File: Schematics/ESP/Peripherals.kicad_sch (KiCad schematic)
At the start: 44 parts, among them J12 Battery Input, J3 Battery charger, J4 Motor A, J5 Motor B, J6 Fan, Q17 PJP18N20, SW1 SW_SPDT, U4 DRV8871DDA, U5 LM2596S-5, U6 DRV8871DDA

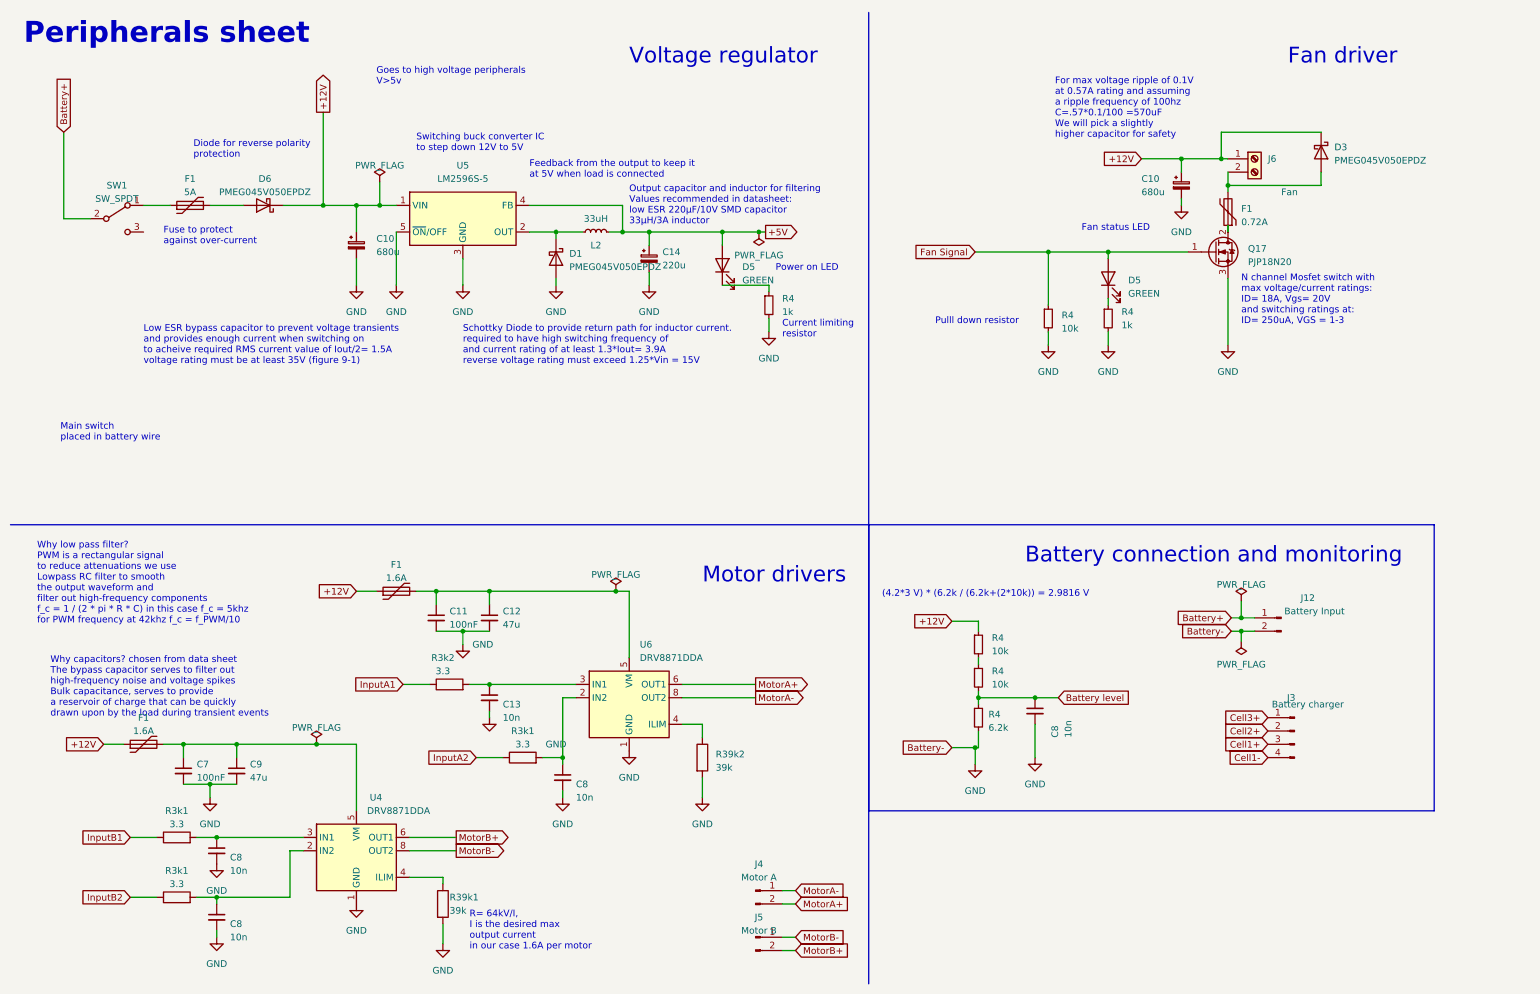
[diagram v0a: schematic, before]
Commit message: added esp32 connected
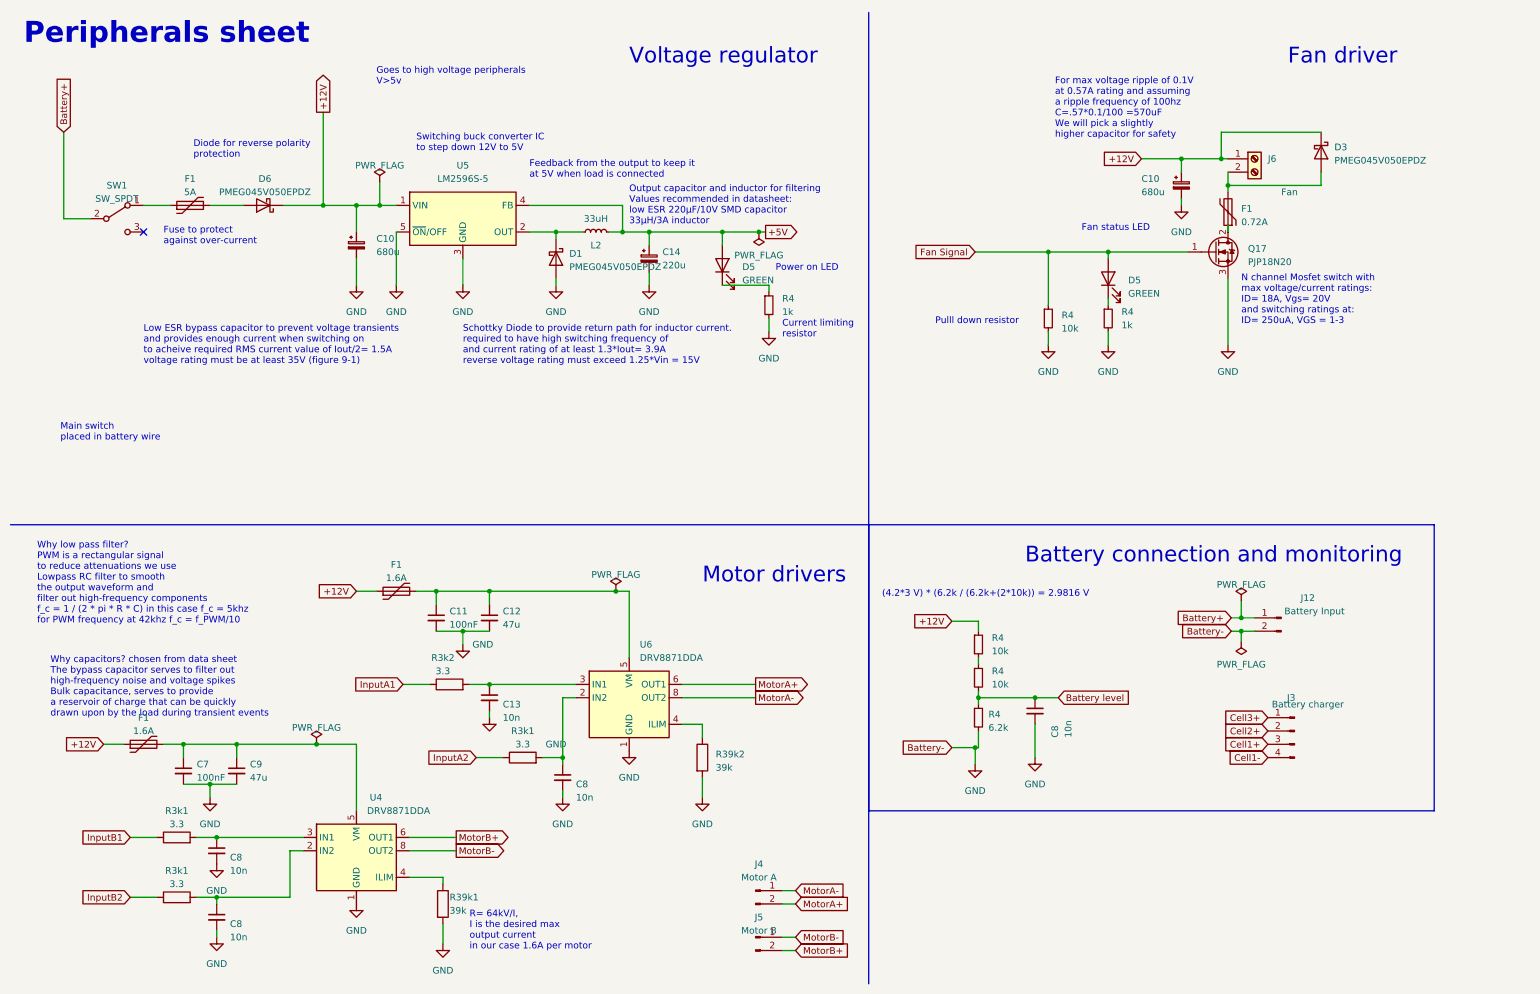
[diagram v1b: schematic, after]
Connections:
- no-connect marks 0 -> 1
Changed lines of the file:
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@@
   (junction (at 99.06 130.81) (diameter 0) (color 0 0 0 0)
   )
+  (no_connect (at 38.1 54.61))
   (wire (pts (xy 64.77 49.53) (xy 72.39 49.53))
     (stroke (width 0) (type default))
@@
     (stroke (width 0) (type default))
   )
-  (wire (pts (xy 196.85 153.035) (xy 192.405 153.035))
-    (stroke (width 0) (type default))
-  )
   (wire (pts (xy 245.745 128.27) (xy 247.65 128.27))
     (stroke (width 0) (type default))
@@
     (stroke (width 0) (type default))
   )
+  (wire (pts (xy 192.405 153.035) (xy 196.85 153.035))
+    (stroke (width 0) (type default))
+  )
   (wire (pts (xy 127 54.61) (xy 129.54 54.61))
     (stroke (width 0) (type default))
@@
     (stroke (width 0) (type default))
   )
-  (wire (pts (xy 196.85 156.21) (xy 196.85 153.035))
-    (stroke (width 0) (type default))
-  )
+  (wire (pts (xy 196.85 153.035) (xy 196.85 156.21))
+    (stroke (width 0) (type default))
+  )

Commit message: fixed bom
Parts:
- F1: Price 0,39 -> 0,32; digikey link https://www.digikey.fi/en/products/detail/bel-fuse-inc/0ZCG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 -> https://www.digikey.com/en/products/detail/bel-fuse-inc/068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
- J12, J3: digikey link (none) -> https://www.digikey.com/en/products/detail/sullins-connecto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
- SW1: digikey link (none) -> https://www.digikey.fi/fi/products/detail/e-switch/500SSP1S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
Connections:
- net Cell1- is gone; now on net GND: J3.4 (Pin_4)
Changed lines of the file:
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@@
+    )
+  )
+  (global_label "Battery-" (shape input) (at 252.73 154.94 180) (fields_autoplaced)
+    (effects (font (size 1.27 1.27)) (justify right))
+    (property "Intersheetrefs" "${INTERSHEET_REFS}" (at 241.539 154.94 0)
+      (effects (font (size 1.27 1.27)) (justify right) hide)
     )
   )
@@
     (property "Intersheetrefs" "${INTERSHEET_REFS}" (at 165.2755 143.4306 0)
       (effects (font (size 1.27 1.27)) (justify left) hide)
-    )
-  )
-  (global_label "Cell1-" (shape input) (at 252.73 154.94 180) (fields_autoplaced)
-    (effects (font (size 1.27 1.27)) (justify right))
-    (property "Intersheetrefs" "${INTERSHEET_REFS}" (at 243.3533 154.94 0)
-      (effects (font (size 1.27 1.27)) (justify right) hide)
     )
   )
@@
       (effects (font (size 1.27 1.27)) hide)
     )
+    (property "digikey link" "https://www.digikey.com/en/products/detail/sullins-connector-solutions/PPTC041LFBN-RC/810144" (at 257.81 149.86 0)
+      (effects (font (size 1.27 1.27)) hide)
+    )
     (pin "1")
     (pin "2")
@@
       (effects (font (size 1.27 1.27)) hide)
     )
-    (property "digikey link" "https://www.digikey.fi/en/products/detail/bel-fuse-inc/0ZCG0260BF2B/4156115" (at 46.99 49.53 90)
-      (effects (font (size 1.27 1.27)) hide)
-    )
-    (property "Price" "0,39" (at 46.99 49.53 0)
+    (property "digikey link" "https://www.digikey.com/en/products/detail/bel-fuse-inc/0685T5000-01/5466711?s=N4IgTCBcDaIAwDYAcBWAKiuWC0cCMIAugL5A" (at 46.99 49.53 90)
+      (effects (font (size 1.27 1.27)) hide)
+    )
+    (property "Price" "0,32" (at 46.99 49.53 0)
       (effects (font (size 1.27 1.27)) hide)
     )
@@
       (effects (font (size 1.27 1.27)) hide)
     )
+    (property "digikey link" "https://www.digikey.com/en/products/detail/sullins-connector-solutions/PPTC021LFBN-RC/810142" (at 255.27 128.27 0)
+      (effects (font (size 1.27 1.27)) hide)
+    )
     (pin "1")
     (pin "2")
@@
       (effects (font (size 1.27 1.27)) hide)
     )
+    (property "digikey link" "https://www.digikey.fi/fi/products/detail/e-switch/500SSP1S1M6QEA/378947?s=N4IgTCBcDaIKwAYEGVkAUCMyMFkBsAigKICCIAugL5A" (at 33.02 52.07 0)
+      (effects (font (size 1.27 1.27)) hide)
+    )

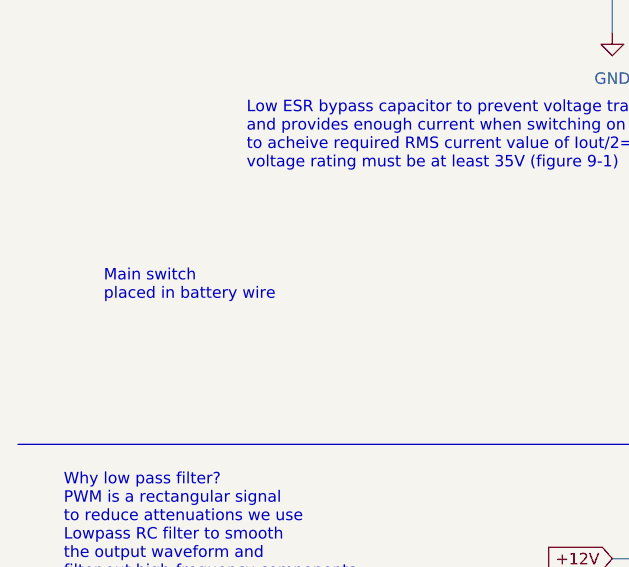
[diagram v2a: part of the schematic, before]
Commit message: charging IC PCB and cleanup
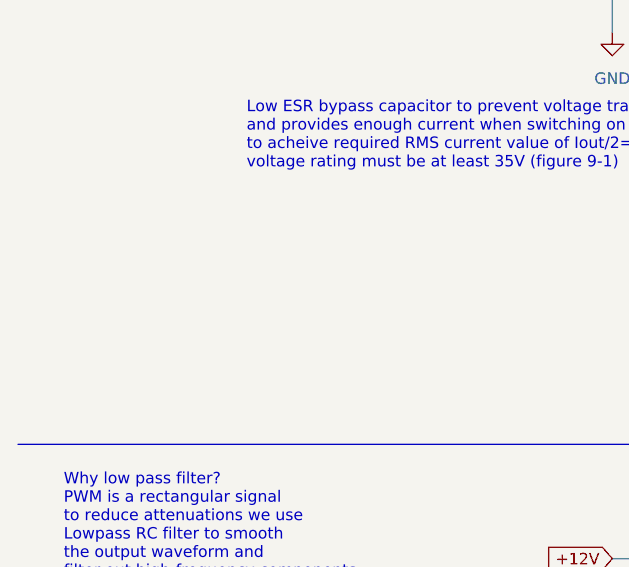
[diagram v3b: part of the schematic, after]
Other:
- note removed: "Main switch placed in battery wire"
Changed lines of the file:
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@@
     (effects (font (size 3 3)) (justify left bottom))
-  )
-  (text "Main switch\nplaced in battery wire" (at 22.225 94.615 0)
-    (effects (font (size 1.27 1.27)) (justify left bottom))
   )
   (text "Feedback from the output to keep it \nat 5V when load is connected"

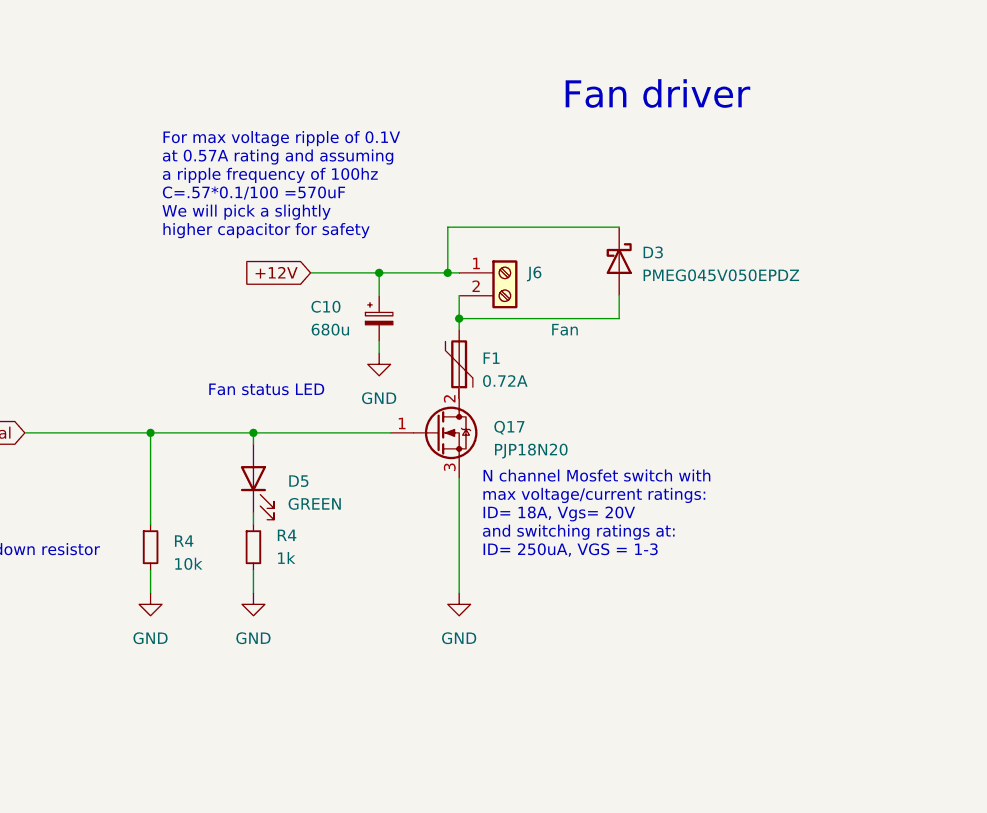
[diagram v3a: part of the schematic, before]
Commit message: removed fan related stuff
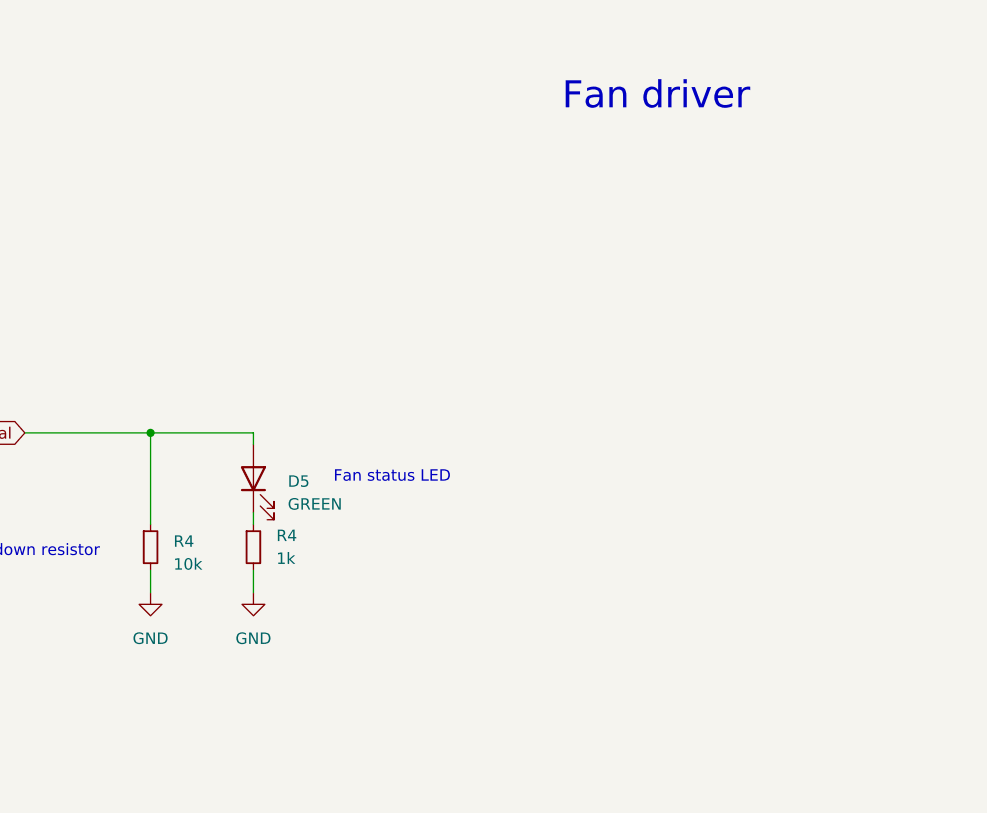
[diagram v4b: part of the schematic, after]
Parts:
- removed C10: 680u, Capacitor_THT:CP_Radial_D10.0mm_P5.00mm, symbol Device:C_Polarized_Small
- removed D3: PMEG045V050EPDZ, Diode_SMD:D_SMB, symbol Device:D_Schottky
- removed F1: 0.72A, Fuse:Fuse_1206_3216Metric_Pad1.42x1.75mm_HandSolder, symbol Device:Polyfuse
- removed J6: Fan, TerminalBlock_Phoenix:TerminalBlock_Phoenix_PT-1,5-2-5.0-H_1x02_P5.00mm_Horizontal, symbol Connector:Screw_Terminal_01x02
- removed Q17: PJP18N20, Package_TO_SOT_THT:TO-220-3_Vertical, symbol Transistor_FET:IRF540N
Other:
- note removed: "For max voltage ripple of 0.1V at 0.57A rating and assuming a ripple frequency of 100hz C=.57*0.1/100 =570uF We will pick a slightly higher capacitor for safety"
- note removed: "N channel Mosfet switch with max voltage/current ratings: ID= 18A, Vgs= 20V and switching ratings at: ID= 250uA, VGS = 1-3"

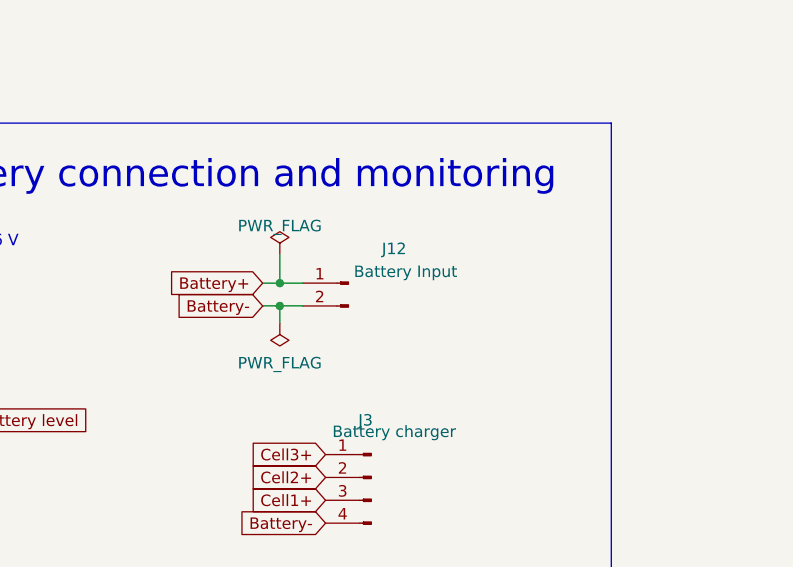
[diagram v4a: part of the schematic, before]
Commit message: fixed 3.3v for IMU
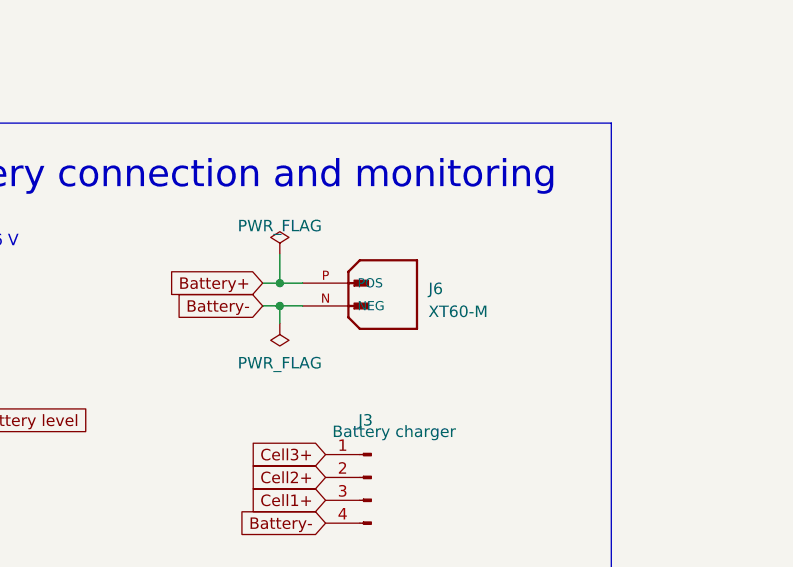
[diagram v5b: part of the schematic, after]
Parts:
- removed J12: Battery Input, Connector_PinSocket_2.54mm:PinSocket_1x02_P2.54mm_Vertical, symbol Connector:Conn_01x02_Pin
- added J6: XT60-M, AMASS_XT60-M, symbol XT60-M:XT60-M
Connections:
- net Battery+: now also J6.P (POS)
- net GND: now also J6.N (NEG)
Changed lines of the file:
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@@
-    )
-  )
-  (symbol (lib_id "Connector:Conn_01x02_Pin") (at 255.27 128.27 0) (mirror y) (unit 1)
-    (in_bom yes) (on_board yes) (dnp no)
-    (property "Reference" "J12" (at 260.35 124.46 0)
-      (effects (font (size 1.27 1.27)))
-    )
-    (property "Value" "Battery Input" (at 261.62 127 0)
-      (effects (font (size 1.27 1.27)))
-    )
-    (property "Footprint" "Connector_PinSocket_2.54mm:PinSocket_1x02_P2.54mm_Vertical" (at 255.27 128.27 0)
-      (effects (font (size 1.27 1.27)) hide)
-    )
-    (property "Datasheet" "~" (at 255.27 128.27 0)
-      (effects (font (size 1.27 1.27)) hide)
-    )
-    (property "digikey link" "https://www.digikey.com/en/products/detail/sullins-connector-solutions/PPTC021LFBN-RC/810142" (at 255.27 128.27 0)
-      (effects (font (size 1.27 1.27)) hide)
-    )
-    (pin "1")
-    (pin "2")
-    (instances
-      (project "ESP"
-        (path "/b616d203-cf5c-462f-b907-860a8573592a/d73e0648-2dfb-47f8-9e43-38f378a4f4ca"
-          (reference "J12") (unit 1)
-        )
-        (path "/b616d203-cf5c-462f-b907-860a8573592a/9ad1e8da-d13f-4a6e-8aa2-8655a1d493de"
-          (reference "J13") (unit 1)
-        )
-      )
     )
   )
@@
         )
       )
+    )
+  )
+  (symbol (lib_id "XT60-M:XT60-M") (at 255.27 130.81 0) (unit 1)
+    (in_bom yes) (on_board yes) (dnp no) (fields_autoplaced)
+    (property "Reference" "J6" (at 264.16 128.905 0)
+      (effects (font (size 1.27 1.27)) (justify left))
+    )
+    (property "Value" "XT60-M" (at 264.16 131.445 0)
+      (effects (font (size 1.27 1.27)) (justify left))
+    )
+    (property "Footprint" "AMASS_XT60-M" (at 255.27 130.81 0)
+      (effects (font (size 1.27 1.27)) (justify bottom) hide)
+    )
+    (property "Datasheet" "" (at 255.27 130.81 0)
+      (effects (font (size 1.27 1.27)) hide)
+    )
+    (property "MAXIMUM_PACKAGE_HEIGHT" "16.00 mm" (at 255.27 130.81 0)
+      (effects (font (size 1.27 1.27)) (justify bottom) hide)
+    )
+    (property "PARTREV" "V1.2" (at 255.27 130.81 0)
+      (effects (font (size 1.27 1.27)) (justify bottom) hide)
+    )
+    (property "MANUFACTURER" "AMASS" (at 255.27 130.81 0)
+      (effects (font (size 1.27 1.27)) (justify bottom) hide)
+    )
+    (property "STANDARD" "IPC 7351B" (at 255.27 130.81 0)
+      (effects (font (size 1.27 1.27)) (justify bottom) hide)
+    )
+    (pin "N")
+    (pin "P")
+    (instances
+      (project "ESP"
+        (path "/b616d203-cf5c-462f-b907-860a8573592a/9ad1e8da-d13f-4a6e-8aa2-8655a1d493de"
+          (reference "J6") (unit 1)
+        )
+      )
